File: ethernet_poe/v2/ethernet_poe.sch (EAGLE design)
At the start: 88 parts, among them J3 ARJM11C7-104-AB-EW2, Q1 BSR16, U1 AZ1117EH-3.3TRG1, U2 IFX91041, U3 W5500, U4 TPS26600PWPR, X1 25MHz

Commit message: Began design review changes
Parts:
- added D7: YLW, led:LEDCHIP-LED0603
- added D8: BLU, led:LEDCHIP-LED0603
- added D9: 1N4148W-7-F, ethernet_poe:1N4148W-7-F
- added R35, R36: 470, rcl:R-US_R0603
- C16: value 1 uF -> 1uF
- C19: value 10nF, 50V -> 10000pF, 50V
- C22, C24, C25, C26: value 10nF -> 10000pF
- R18: value 600 -> 330
- R19: value 220 -> 470
- R23, R8: value 49 -> 49, 1%
- R24: value 22 -> 22, 1%
- R29, R3: value 75 -> 75, 1%
- R30: value 715k -> 715k, 1%
- R31: value 20k -> 20k, 1%
- R32: value 30.1k -> 30.1k, 1%
- R33: value 11.8k 1% -> 11.8k, 1%
- R34: value 33.2k -> 66.5k, 1%
- R4: value 12.4k 1% -> 12.4k, 1%
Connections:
- net !SCSN renamed !SCS
- net N$14 renamed 5V_RAW
- net N$29 renamed CT
- net N$30 renamed Y_LED+
- net N$31 renamed G_LED+
- net N$32 renamed RTN
- new net 3V3_LED1: D7.A, R35.2
- new net 3V3_LED2: D8.A, R36.2
- new net ACTLED: D7.C, U3.ACTLED
- new net DUPLED: D8.C, U3.DUPLED
- net +3V3_D: now also D9.2, R35.1, R36.1
- net +5V: now also D9.1
- net AGND: now also J3.CHASSIS1, J3.CHASSIS2; no longer J3.CH1, J3.CH2
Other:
- note added: "#3 (or M2.5) Drill Size"
- note added: "1.8A Rated"
- note added: "R34 = V(IMONmax)/(I(ILIM)*75*10^-6) V(IMONmax) = max ADC voltage = 5V"
- moved on the sheet: D3, D5, D6, R10, R11, R12, R13, R14, R17, R18, R19, R9

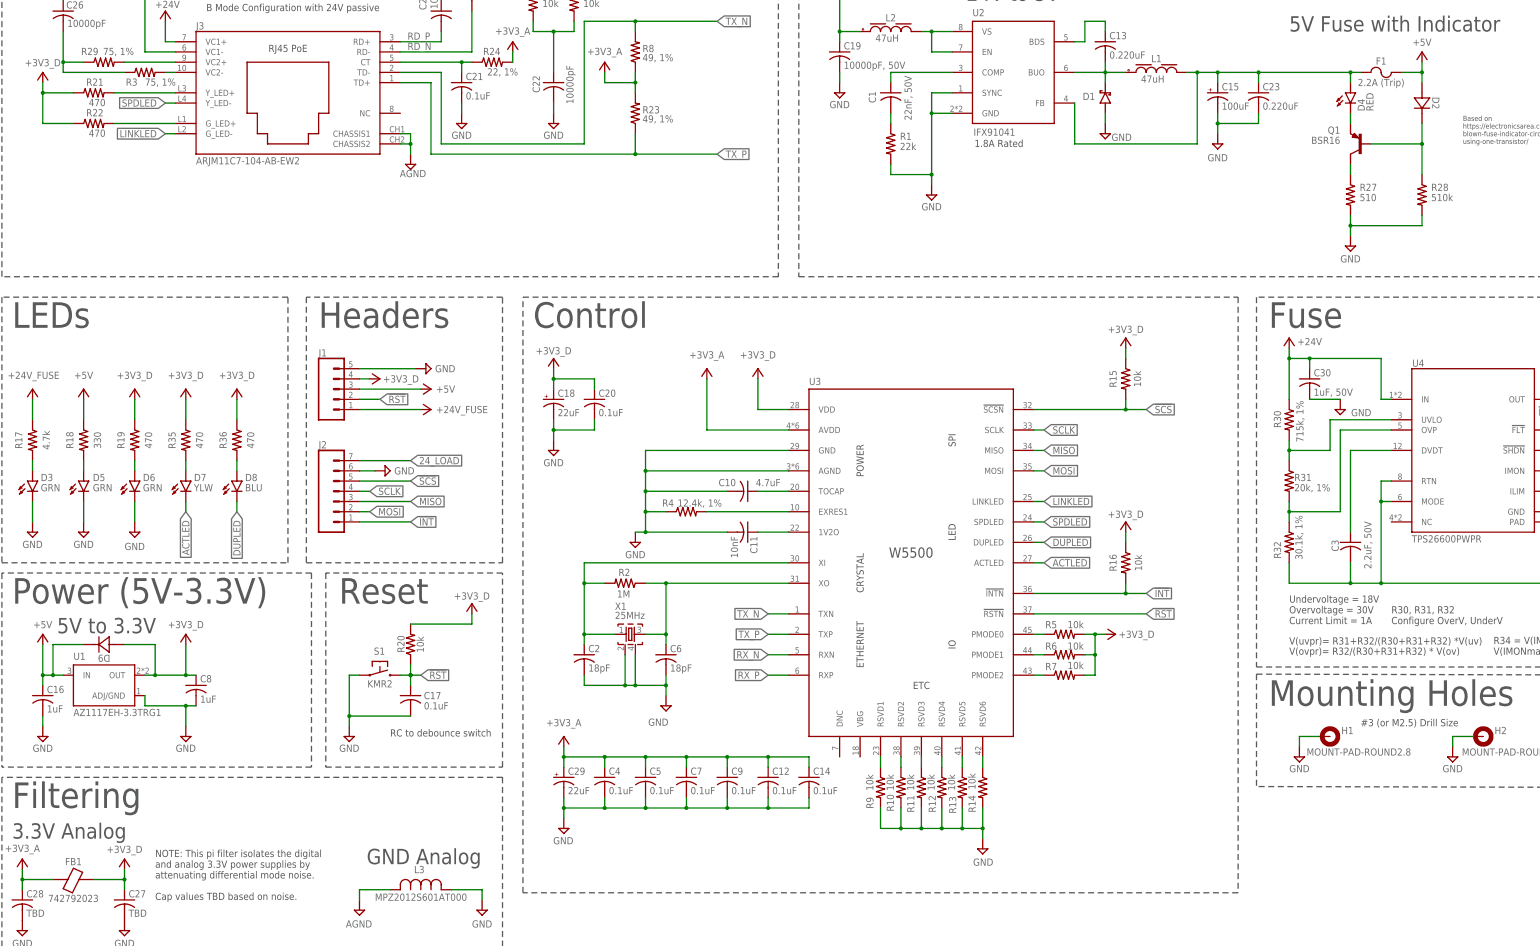
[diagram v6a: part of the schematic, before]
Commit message: post design review routing updates
replaced 5V DC/DC converter catch diode
routed Wiznet LEDs
added thermal pads to efuse and DC/DC converters
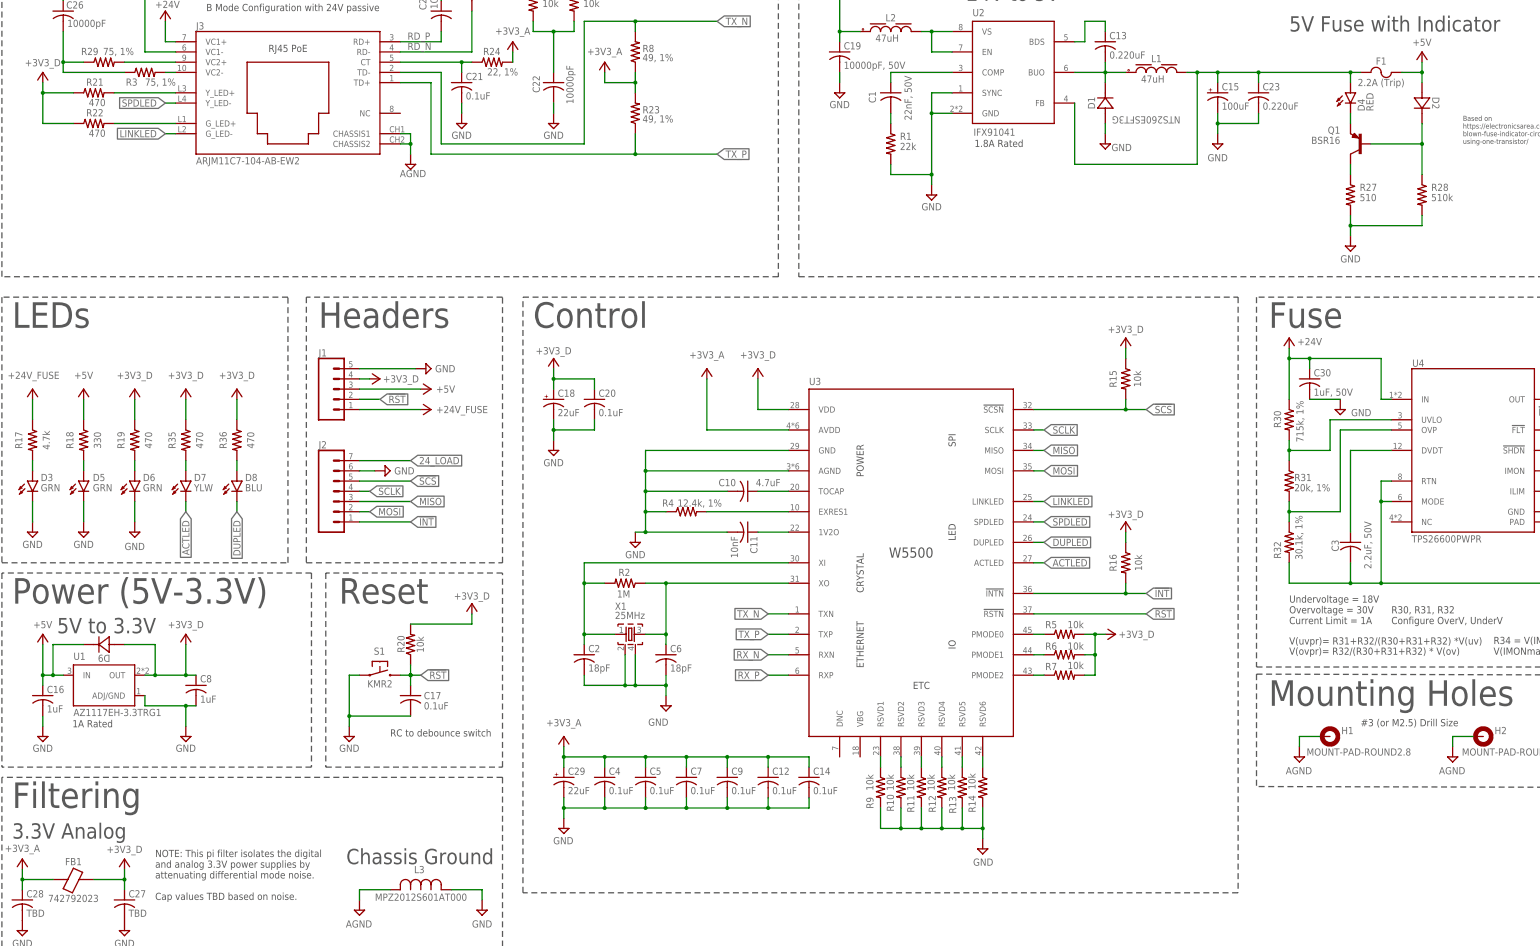
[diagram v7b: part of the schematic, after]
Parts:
- D1: value (none) -> NTS260ESFT3G; device RoboJackets-Diodes:SCHOTTKYSOD-323 -> ethernet_poe:NTS260ESFT3G
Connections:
- net 5V_RAW: now also D1.1; no longer D1.C
- net AGND: now also H1.MOUNT, H2.MOUNT
- net GND: now also D1.2; no longer D1.A, H1.MOUNT, H2.MOUNT
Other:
- note added: "1A Rated"
- note added: "Chassis Ground"
- note removed: "GND Analog"
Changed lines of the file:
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@@
 <?xml version="1.0" encoding="utf-8"?>
 <!DOCTYPE eagle SYSTEM "eagle.dtd">
-<eagle version="9.6.2">
+<eagle version="9.5.2">
 <drawing>
 <settings>
@@
 <part name="SUPPLY3" library="supply2" library_urn="urn:adsk.eagle:library:372" deviceset="GND" device=""/>
 <part name="C13" library="rcl" library_urn="urn:adsk.eagle:library:334" deviceset="C-US" device="C0603" package3d_urn="urn:adsk.eagle:package:23616/2" value="0.220uF"/>
-<part name="D1" library="RoboJackets-Diodes" deviceset="SCHOTTKY" device="SOD-323"/>
 <part name="SUPPLY6" library="supply2" library_urn="urn:adsk.eagle:library:372" deviceset="GND" device=""/>
 <part name="C1" library="rcl" library_urn="urn:adsk.eagle:library:334" deviceset="C-US" device="C0603" package3d_urn="urn:adsk.eagle:package:23616/2" value="22nF, 50V"/>
@@
 <part name="+24V_FUSE3" library="ethernet_poe" deviceset="+24V_FUSE" device=""/>
 <part name="+24V_FUSE4" library="ethernet_poe" deviceset="+24V_FUSE" device=""/>
-<part name="SUPPLY31" library="supply2" library_urn="urn:adsk.eagle:library:372" deviceset="GND" device=""/>
 <part name="H1" library="holes" library_urn="urn:adsk.eagle:library:237" deviceset="MOUNT-PAD-ROUND" device="2.8" package3d_urn="urn:adsk.eagle:package:14281/1"/>
 <part name="H2" library="holes" library_urn="urn:adsk.eagle:library:237" deviceset="MOUNT-PAD-ROUND" device="2.8" package3d_urn="urn:adsk.eagle:package:14281/1"/>
-<part name="SUPPLY32" library="supply2" library_urn="urn:adsk.eagle:library:372" deviceset="GND" device=""/>
 <part name="FRAME1" library="RoboJackets-Frames" deviceset="FRAME_11_17" device="">
 <attribute name="REVISION" value="2.0"/>
@@
 <part name="+3V3_D13" library="ethernet_poe" deviceset="+3V3_D" device=""/>
 <part name="D9" library="ethernet_poe" deviceset="1N4148W-7-F" device=""/>
+<part name="SUPPLY31" library="supply2" library_urn="urn:adsk.eagle:library:372" deviceset="AGND" device=""/>
+<part name="SUPPLY32" library="supply2" library_urn="urn:adsk.eagle:library:372" deviceset="AGND" device=""/>
+<part name="D1" library="ethernet_poe" deviceset="NTS260ESFT3G" device=""/>
 </parts>
 <sheets>
@@
 <wire x1="84.582" y1="101.6" x2="84.582" y2="53.34" width="0.1524" layer="97" style="shortdash"/>
 <text x="10.16" y="43.18" size="6.35" layer="97" ratio="12">Filtering</text>
-<text x="98.298" y="29.21" size="3.81" layer="97">GND Analog</text>
+<text x="93.218" y="29.21" size="3.81" layer="97">Chassis Ground</text>
 <wire x1="7.62" y1="50.8" x2="7.62" y2="2.54" width="0.1524" layer="97" style="shortdash"/>
 <wire x1="132.08" y1="50.8" x2="7.62" y2="50.8" width="0.1524" layer="97" style="shortdash"/>
@@
 <text x="249.428" y="207.518" size="1.778" layer="97">1.8A Rated</text>
 <text x="345.44" y="63.5" size="1.778" layer="97">#3 (or M2.5) Drill Size</text>
+<text x="25.146" y="63.246" size="1.778" layer="97">1A Rated</text>
 </plain>
 <instances>
@@
 <attribute name="VALUE" x="282.956" y="229.489" size="1.778" layer="96"/>
 </instance>
-<instance part="D1" gate="G$1" x="281.94" y="220.98" smashed="yes">
-<attribute name="NAME" x="279.4" y="220.98" size="1.778" layer="95" rot="R180"/>
-<attribute name="VALUE" x="284.48" y="218.44" size="1.778" layer="96"/>
-</instance>
-<instance part="SUPPLY6" gate="GND" x="281.94" y="210.82" smashed="yes">
-<attribute name="VALUE" x="286.004" y="210.82" size="1.778" layer="96" align="top-center"/>
+<instance part="SUPPLY6" gate="GND" x="281.94" y="208.28" smashed="yes">
+<attribute name="VALUE" x="286.004" y="208.28" size="1.778" layer="96" align="top-center"/>
 </instance>
 <instance part="C1" gate="G$1" x="228.6" y="220.98" smashed="yes">
@@
 <attribute name="VALUE" x="15.494" y="149.86" size="1.778" layer="96" align="bottom-center"/>
 </instance>
-<instance part="SUPPLY31" gate="GND" x="330.2" y="55.88" smashed="yes">
-<attribute name="VALUE" x="330.2" y="53.848" size="1.778" layer="96" align="top-center"/>
-</instance>
 <instance part="H1" gate="G$1" x="337.82" y="60.96" smashed="yes">
 <attribute name="NAME" x="340.614" y="61.5442" size="1.778" layer="95"/>
@@
 <attribute name="NAME" x="378.714" y="61.5442" size="1.778" layer="95"/>
 <attribute name="VALUE" x="370.586" y="56.2102" size="1.778" layer="96"/>
-</instance>
-<instance part="SUPPLY32" gate="GND" x="368.3" y="55.88" smashed="yes">
-<attribute name="VALUE" x="368.3" y="53.848" size="1.778" layer="96" align="top-center"/>
 </instance>
 <instance part="FRAME1" gate="G$1" x="0" y="0" smashed="yes"/>
@@
 <instance part="D9" gate="A" x="33.02" y="83.82" smashed="yes" rot="R180">
 <attribute name="NAME" x="33.02" y="81.28" size="1.778" layer="95" ratio="10" rot="SR180" align="bottom-center"/>
+</instance>
+<instance part="SUPPLY31" gate="G$1" x="330.2" y="55.88" smashed="yes">
+<attribute name="VALUE" x="330.073" y="53.34" size="1.778" layer="96" align="top-center"/>
+</instance>
+<instance part="SUPPLY32" gate="G$1" x="368.3" y="55.88" smashed="yes">
+<attribute name="VALUE" x="368.173" y="53.34" size="1.778" layer="96" align="top-center"/>
+</instance>
+<instance part="D1" gate="D$1" x="281.94" y="218.44" smashed="yes" rot="R90">
+<attribute name="VALUE" x="292.1" y="213.36" size="1.778" layer="96" ratio="10" rot="SR180" align="top-center"/>
+<attribute name="NAME" x="279.4" y="218.44" size="1.778" layer="95" ratio="10" rot="SR90" align="bottom-center"/>
 </instance>
 </instances>
@@
 <wire x1="243.84" y1="215.9" x2="238.76" y2="215.9" width="0.1524" layer="91"/>
 <junction x="238.76" y="215.9"/>
-</segment>
-<segment>
-<pinref part="D1" gate="G$1" pin="A"/>
-<pinref part="SUPPLY6" gate="GND" pin="GND"/>
-<wire x1="281.94" y1="215.9" x2="281.94" y2="213.36" width="0.1524" layer="91"/>
 </segment>
 <segment>
@@
 </segment>
 <segment>
-<pinref part="SUPPLY31" gate="GND" pin="GND"/>
-<wire x1="330.2" y1="58.42" x2="330.2" y2="60.96" width="0.1524" layer="91"/>
-<pinref part="H1" gate="G$1" pin="MOUNT"/>
-<wire x1="330.2" y1="60.96" x2="335.28" y2="60.96" width="0.1524" layer="91"/>
-</segment>
-<segment>
-<pinref part="SUPPLY32" gate="GND" pin="GND"/>
-<wire x1="368.3" y1="58.42" x2="368.3" y2="60.96" width="0.1524" layer="91"/>
-<pinref part="H2" gate="G$1" pin="MOUNT"/>
-<wire x1="368.3" y1="60.96" x2="373.38" y2="60.96" width="0.1524" layer="91"/>
-</segment>
-<segment>
 <pinref part="S1" gate="G$1" pin="1"/>
 <wire x1="93.98" y1="66.04" x2="93.98" y2="76.2" width="0.1524" layer="91"/>
@@
 <junction x="93.98" y="66.04"/>
 <pinref part="SUPPLY19" gate="GND" pin="GND"/>
+</segment>
+<segment>
+<pinref part="SUPPLY6" gate="GND" pin="GND"/>
+<wire x1="281.94" y1="210.82" x2="281.94" y2="213.36" width="0.1524" layer="91"/>
+<pinref part="D1" gate="D$1" pin="2"/>
 </segment>
 </net>
@@
 <wire x1="281.94" y1="228.6" x2="281.94" y2="226.06" width="0.1524" layer="91"/>
 <junction x="281.94" y="226.06"/>
-<pinref part="D1" gate="G$1" pin="C"/>
 <wire x1="281.94" y1="223.52" x2="281.94" y2="226.06" width="0.1524" layer="91"/>
 <pinref part="U2" gate="G$1" pin="BUO"/>
 <wire x1="274.32" y1="226.06" x2="281.94" y2="226.06" width="0.1524" layer="91"/>
 <pinref part="L1" gate="G$1" pin="1"/>
+<pinref part="D1" gate="D$1" pin="1"/>
 </segment>
 </net>
@@
 <wire x1="304.8" y1="226.06" x2="309.88" y2="226.06" width="0.1524" layer="91"/>
 <wire x1="309.88" y1="226.06" x2="309.88" y2="223.52" width="0.1524" layer="91"/>
-<wire x1="274.32" y1="218.44" x2="274.32" y2="208.28" width="0.1524" layer="91"/>
-<wire x1="274.32" y1="208.28" x2="304.8" y2="208.28" width="0.1524" layer="91"/>
-<wire x1="304.8" y1="208.28" x2="304.8" y2="226.06" width="0.1524" layer="91"/>
+<wire x1="274.32" y1="218.44" x2="274.32" y2="203.2" width="0.1524" layer="91"/>
+<wire x1="274.32" y1="203.2" x2="304.8" y2="203.2" width="0.1524" layer="91"/>
+<wire x1="304.8" y1="203.2" x2="304.8" y2="226.06" width="0.1524" layer="91"/>
 <junction x="304.8" y="226.06"/>
 <pinref part="C15" gate="G$1" pin="+"/>
@@
 <wire x1="104.14" y1="22.86" x2="96.52" y2="22.86" width="0.1524" layer="91"/>
 </segment>
-</net>
+<segment>
+<wire x1="330.2" y1="58.42" x2="330.2" y2="60.96" width="0.1524" layer="91"/>
+<pinref part="H1" gate="G$1" pin="MOUNT"/>
+<wire x1="330.2" y1="60.96" x2="335.28" y2="60.96" width="0.1524" layer="91"/>
+<pinref part="SUPPLY31" gate="G$1" pin="AGND"/>
+</segment>
+<segment>
+<wire x1="368.3" y1="58.42" x2="368.3" y2="60.96" width="0.1524" layer="91"/>
+<pinref part="H2" gate="G$1" pin="MOUNT"/>
+<wire x1="368.3" y1="60.96" x2="373.38" y2="60.96" width="0.1524" layer="91"/>
+<pinref part="SUPPLY32" gate="G$1" pin="AGND"/>
+</segment>
+</net>
